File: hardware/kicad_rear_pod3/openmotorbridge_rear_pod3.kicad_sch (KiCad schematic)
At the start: 0 parts

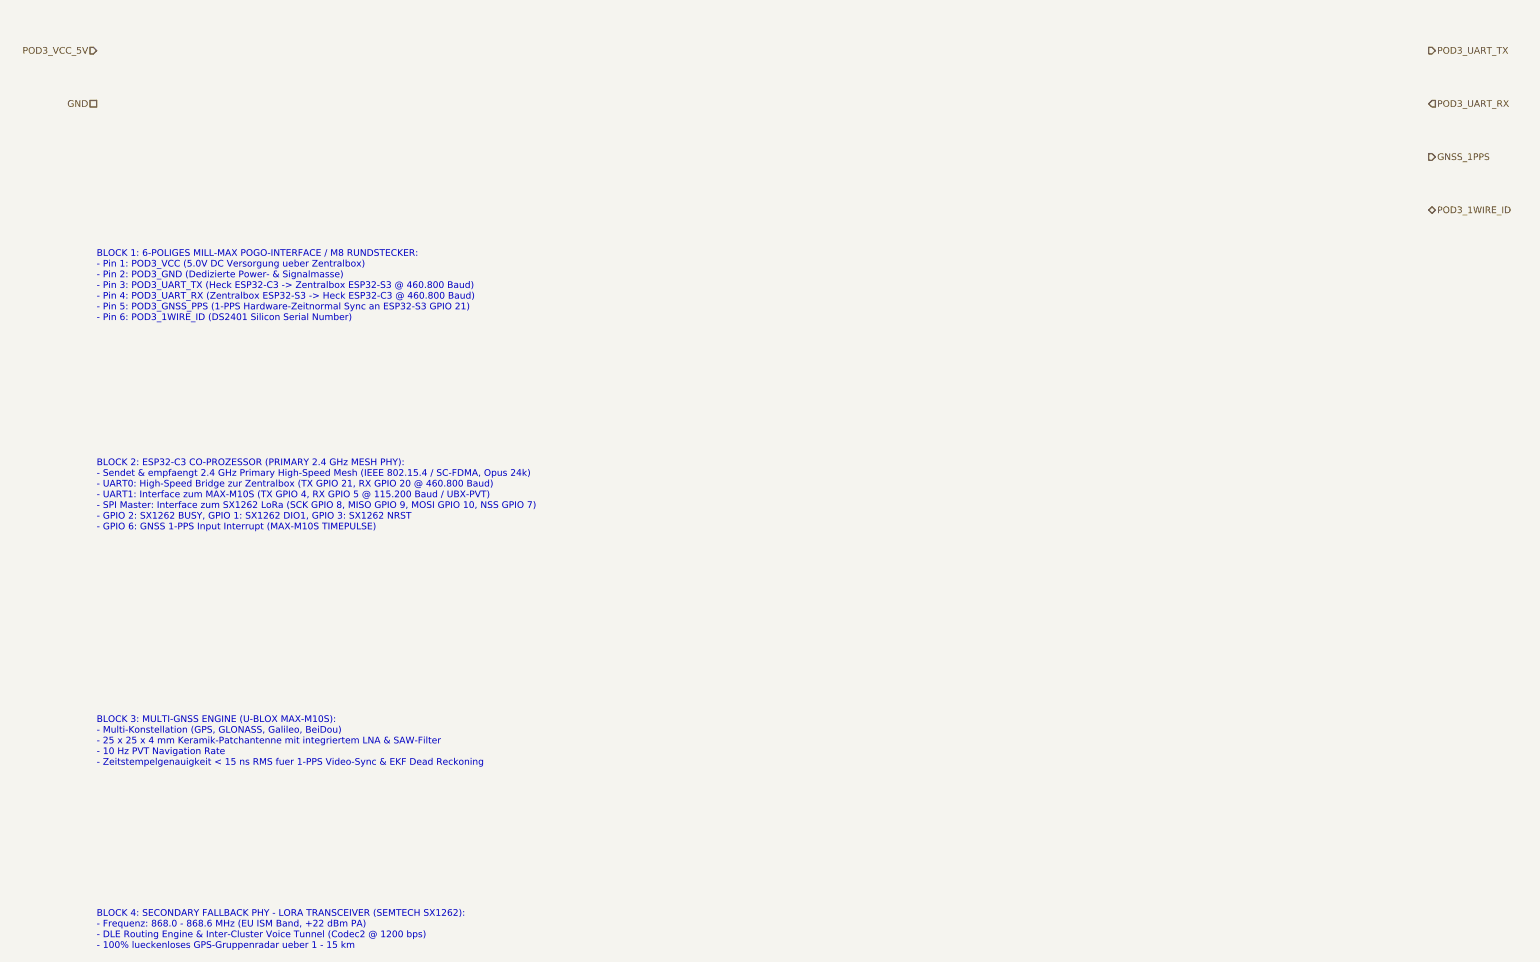
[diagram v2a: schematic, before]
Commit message: feat(kicad): Implement full graphical electronic schematic drawings (symbols, pins, wires, components) for all boards
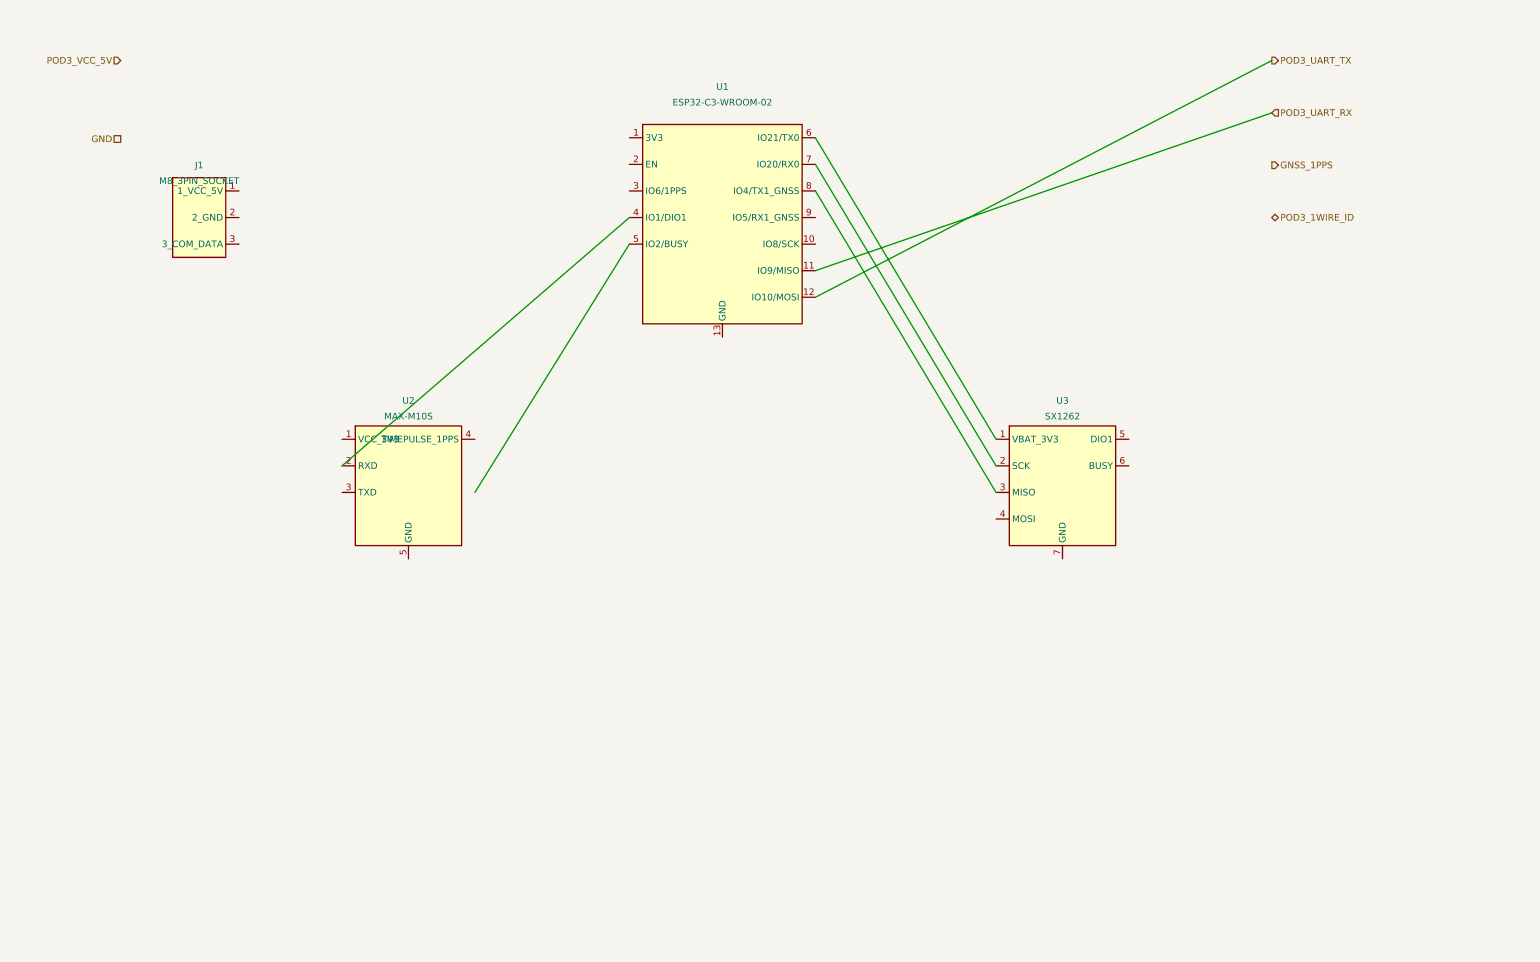
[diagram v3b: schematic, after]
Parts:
- added J1: M8_3PIN_SOCKET, symbol Connector:M8_3Pin
- added U1: ESP32-C3-WROOM-02, symbol RF_Module:ESP32-C3-WROOM-02
- added U2: MAX-M10S, symbol RF_GPS:u-blox_MAX-M10S
- added U3: SX1262, symbol RF_Transceiver:SX1262
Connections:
- net POD3_UART_RX: now also U1.11 (IO9/MISO)
- net POD3_UART_TX: now also U1.12 (IO10/MOSI)
- new net: U1.4 (IO1/DIO1), U2.2 (RXD)
- new net: U1.6 (IO21/TX0), U3.1 (VBAT_3V3)
- new net: U1.7 (IO20/RX0), U3.2 (SCK)
- new net: U1.8 (IO4/TX1_GNSS), U3.3 (MISO)
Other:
- note removed: "BLOCK 1: 6-POLIGES MILL-MAX POGO-INTERFACE / M8 RUNDSTECKER: - Pin 1: POD3_VCC (5.0V DC Versorgung ueber Zentralbox) - Pin 2: POD3_GND (Dedizierte Power- & Signalmasse) - Pin 3: POD3_UART_TX (Heck ESP32-C3 -> Zentralbox ESP32-S3 @ 460.800 Baud) - Pin 4: POD3_UART_RX (Zentralbox ESP32-S3 -> Heck ESP32-C3 @ 460.800 Baud) - Pin 5: POD3_GNSS_PPS (1-PPS Hardware-Zeitnormal Sync an ESP32-S3 GPIO 21) - 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"
- note removed: "BLOCK 2: ESP32-C3 CO-PROZESSOR (PRIMARY 2.4 GHz MESH PHY): - Sendet & empfaengt 2.4 GHz Primary High-Speed Mesh (IEEE 802.15.4 / SC-FDMA, Opus 24k) - UART0: High-Speed Bridge zur Zentralbox (TX GPIO 21, RX GPIO 20 @ 460.800 Baud) - UART1: Interface zum MAX-M10S (TX GPIO 4, RX GPIO 5 @ 115.200 Baud / UBX-PVT) - SPI Master: Interface zum SX1262 LoRa (SCK GPIO 8, MISO GPIO 9, MOSI GPIO 10, NSS GPIO 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"
- note removed: "BLOCK 3: MULTI-GNSS ENGINE (U-BLOX MAX-M10S): - Multi-Konstellation (GPS, GLONASS, Galileo, BeiDou) - 25 x 25 x 4 mm Keramik-Patchantenne mit integriertem LNA & SAW-Filter - 10 Hz PVT Navigation Rate - Zeitstempelgenauigkeit < 15 ns RMS fuer 1-PPS Video-Sync & EKF Dead Reckoning"
- note removed: "BLOCK 4: SECONDARY FALLBACK PHY - LORA TRANSCEIVER (SEMTECH SX1262): - Frequenz: 868.0 - 868.6 MHz (EU ISM Band, +22 dBm PA) - DLE Routing Engine & Inter-Cluster Voice Tunnel (Codec2 @ 1200 bps) - 100% lueckenloses GPS-Gruppenradar ueber 1 - 15 km"
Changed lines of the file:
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@@
-(kicad_sch (version 20260206) (generator "eeschema") (generator_version "10.0")
-  (paper "A3")
-  (title_block
-    (title "OpenMotorBridge v8.0 - Heck-Pod 3 (GNSS & Dual-PHY OpenMotorMesh)")
-    (date "2026-08-24")
-    (rev "v8.0")
-    (company "OpenMotorBridge Open Source Hardware")
-    (comment 1 "u-blox MAX-M10S 10Hz GNSS + ESP32-C3 2.4GHz Mesh + Semtech SX1262 LoRa (+22 dBm @ 868 MHz)")
-    (comment 2 "Dual-PHY OMM Transceiver: 2.4 GHz HiFi Primary + 868 MHz Long-Range Fallback")
-  )
-  (hierarchical_label "POD3_VCC_5V" (shape input) (at 25.4 38.1 180)
-    (effects (font (size 1.27 1.27)) (justify right))
-  )
-  (hierarchical_label "GND" (shape passive) (at 25.4 48.26 180)
-    (effects (font (size 1.27 1.27)) (justify right))
-  )
-  (hierarchical_label "POD3_UART_TX" (shape output) (at 280.0 38.1 0)
-    (effects (font (size 1.27 1.27)) (justify left))
-  )
-  (hierarchical_label "POD3_UART_RX" (shape input) (at 280.0 48.26 0)
-    (effects (font (size 1.27 1.27)) (justify left))
-  )
-  (hierarchical_label "GNSS_1PPS" (shape output) (at 280.0 58.42 0)
-    (effects (font (size 1.27 1.27)) (justify left))
-  )
-  (hierarchical_label "POD3_1WIRE_ID" (shape bidirectional) (at 280.0 68.58 0)
-    (effects (font (size 1.27 1.27)) (justify left))
-  )
-  (text "BLOCK 1: 6-POLIGES MILL-MAX POGO-INTERFACE / M8 RUNDSTECKER:\n- Pin 1: POD3_VCC (5.0V DC Versorgung ueber Zentralbox)\n- Pin 2: POD3_GND (Dedizierte Power- & Signalmasse)\n- Pin 3: POD3_UART_TX (Heck ESP32-C3 -> Zentralbox ESP32-S3 @ 460.800 Baud)\n- Pin 4: POD3_UART_RX (Zentralbox ESP32-S3 -> Heck ESP32-C3 @ 460.800 Baud)\n- Pin 5: POD3_GNSS_PPS (1-PPS Hardware-Zeitnormal Sync an ESP32-S3 GPIO 21)\n- Pin 6: POD3_1WIRE_ID (DS2401 Silicon Serial Number)" (at 25.4 90.0 0)
-    (effects (font (size 1.27 1.27)) (justify left bottom))
-  )
-  (text "BLOCK 2: ESP32-C3 CO-PROZESSOR (PRIMARY 2.4 GHz MESH PHY):\n- Sendet & empfaengt 2.4 GHz Primary High-Speed Mesh (IEEE 802.15.4 / SC-FDMA, Opus 24k)\n- UART0: High-Speed Bridge zur Zentralbox (TX GPIO 21, RX GPIO 20 @ 460.800 Baud)\n- UART1: Interface zum MAX-M10S (TX GPIO 4, RX GPIO 5 @ 115.200 Baud / UBX-PVT)\n- SPI Master: Interface zum SX1262 LoRa (SCK GPIO 8, MISO GPIO 9, MOSI GPIO 10, NSS GPIO 7)\n- GPIO 2: SX1262 BUSY, GPIO 1: SX1262 DIO1, GPIO 3: SX1262 NRST\n- GPIO 6: GNSS 1-PPS Input Interrupt (MAX-M10S TIMEPULSE)" (at 25.4 130.0 0)
-    (effects (font (size 1.27 1.27)) (justify left bottom))
-  )
-  (text "BLOCK 3: MULTI-GNSS ENGINE (U-BLOX MAX-M10S):\n- Multi-Konstellation (GPS, GLONASS, Galileo, BeiDou)\n- 25 x 25 x 4 mm Keramik-Patchantenne mit integriertem LNA & SAW-Filter\n- 10 Hz PVT Navigation Rate\n- Zeitstempelgenauigkeit < 15 ns RMS fuer 1-PPS Video-Sync & EKF Dead Reckoning" (at 25.4 175.0 0)
-    (effects (font (size 1.27 1.27)) (justify left bottom))
-  )
-  (text "BLOCK 4: SECONDARY FALLBACK PHY - LORA TRANSCEIVER (SEMTECH SX1262):\n- Frequenz: 868.0 - 868.6 MHz (EU ISM Band, +22 dBm PA)\n- DLE Routing Engine & Inter-Cluster Voice Tunnel (Codec2 @ 1200 bps)\n- 100% lueckenloses GPS-Gruppenradar ueber 1 - 15 km" (at 25.4 210.0 0)
-    (effects (font (size 1.27 1.27)) (justify left bottom))
-  )
+(kicad_sch
+	(version 20260206)
+	(generator "eeschema")
+	(generator_version "10.0")
+	(paper "A3")
+	(title_block
+		(title "OpenMotorBridge v8.0 - Heck-Pod 3 (GNSS & Dual-PHY OpenMotorMesh)")
+		(date "2026-08-24")
+		(rev "v8.0")
+		(company "OpenMotorBridge Open Source Hardware")
+		(comment 1 "u-blox MAX-M10S 10Hz GNSS + ESP32-C3 2.4GHz Mesh + Semtech SX1262 LoRa (+22 dBm @ 868 MHz)")
+		(comment 2 "Dual-PHY OMM Transceiver: 2.4 GHz HiFi Primary + 868 MHz Long-Range Fallback")
+	)
+	;; =========================================================================
+	;; Hierarchical Labels
+	;; =========================================================================
+	(hierarchical_label "POD3_VCC_5V" (shape input) (at 30.0 40.0 180) (effects (font (size 1.27 1.27)) (justify right)))
+	(hierarchical_label "GND" (shape passive) (at 30.0 55.0 180) (effects (font (size 1.27 1.27)) (justify right)))
+	(hierarchical_label "POD3_UART_TX" (shape output) (at 250.0 40.0 0) (effects (font (size 1.27 1.27)) (justify left)))
+	(hierarchical_label "POD3_UART_RX" (shape input) (at 250.0 50.0 0) (effects (font (size 1.27 1.27)) (justify left)))
+	(hierarchical_label "GNSS_1PPS" (shape output) (at 250.0 60.0 0) (effects (font (size 1.27 1.27)) (justify left)))
+	(hierarchical_label "POD3_1WIRE_ID" (shape bidirectional) (at 250.0 70.0 0) (effects (font (size 1.27 1.27)) (justify left)))
+	;; =========================================================================
+	;; Symbols Placement
+	;; =========================================================================
+	;; J1: M8 Connector
+	(symbol (lib_id "Connector:M8_3Pin") (at 45.0 70.0 0) (unit 1)
+		(in_bom yes) (on_board yes) (dnp no)
+		(property "Reference" "J1" (at 45.0 60.0 0) (effects (font (size 1.27 1.27))))
+		(property "Value" "M8_3PIN_SOCKET" (at 45.0 63.0 0) (effects (font (size 1.27 1.27))))
+		(pin "1")
+		(pin "2")
+		(pin "3")
+	)
+	;; U2: MAX-M10S GNSS Engine
+	(symbol (lib_id "RF_GPS:u-blox_MAX-M10S") (at 85.0 120.0 0) (unit 1)
+		(in_bom yes) (on_board yes) (dnp no)
+		(property "Reference" "U2" (at 85.0 105.0 0) (effects (font (size 1.27 1.27))))
+		(property "Value" "MAX-M10S" (at 85.0 108.0 0) (effects (font (size 1.27 1.27))))
+		(pin "1")
+		(pin "2")
+		(pin "3")
+		(pin "4")
+		(pin "5")
+	)
+	;; U1: ESP32-C3 Co-Processor
+	(symbol (lib_id "RF_Module:ESP32-C3-WROOM-02") (at 145.0 70.0 0) (unit 1)
+		(in_bom yes) (on_board yes) (dnp no)
+		(property "Reference" "U1" (at 145.0 45.0 0) (effects (font (size 1.27 1.27))))
+		(property "Value" "ESP32-C3-WROOM-02" (at 145.0 48.0 0) (effects (font (size 1.27 1.27))))
+		(pin "1")
+		(pin "2")
+		(pin "3")
+		(pin "4")
+		(pin "5")
+		(pin "6")
+		(pin "7")
+		(pin "8")
+		(pin "9")
+		(pin "10")
+		(pin "11")
+		(pin "12")
+		(pin "13")
+	)
+	;; U3: SX1262 LoRa Transceiver
+	(symbol (lib_id "RF_Transceiver:SX1262") (at 210.0 120.0 0) (unit 1)
+		(in_bom yes) (on_board yes) (dnp no)
+		(property "Reference" "U3" (at 210.0 105.0 0) (effects (font (size 1.27 1.27))))
+		(property "Value" "SX1262" (at 210.0 108.0 0) (effects (font (size 1.27 1.27))))
+		(pin "1")
+		(pin "2")
+		(pin "3")
+		(pin "4")
+		(pin "5")
+		(pin "6")
+		(pin "7")
+	)
+	;; Wires
+	;; UART bridge to Central Box
+	(wire (pts (xy 162.78 85.24) (xy 250.0 40.0)) (stroke (width 0) (type solid)))
+	(wire (pts (xy 162.78 80.16) (xy 250.0 50.0)) (stroke (width 0) (type solid)))
+	;; SPI to LoRa
+	(wire (pts (xy 162.78 64.92) (xy 197.3 122.54)) (stroke (width 0) (type solid)))
+	(wire (pts (xy 162.78 59.84) (xy 197.3 117.46)) (stroke (width 0) (type solid)))
+	(wire (pts (xy 162.78 54.76) (xy 197.3 112.38)) (stroke (width 0) (type solid)))
+	;; GNSS to ESP32-C3
+	(wire (pts (xy 97.7 122.54) (xy 127.22 75.08)) (stroke (width 0) (type solid)))
+	(wire (pts (xy 72.3 117.46) (xy 127.22 70.0)) (stroke (width 0) (type solid)))
 )
